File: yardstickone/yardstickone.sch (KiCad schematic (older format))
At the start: 68 parts, among them J1 USB-DEVICE, P1 CONN_02X07, P2 SMA-EDGE, P3 RESET_N, P4 DD, P5 DC, P6 3V3, P7 GND, T1 BALUN, U1 CC1111, U2 AP7313, U3 DMC2400, U4 RX_AMP, U5 SKY13385, U6 SKY13385, U7 TX_AMP, U8 DMC2400, X1 CRYSTAL

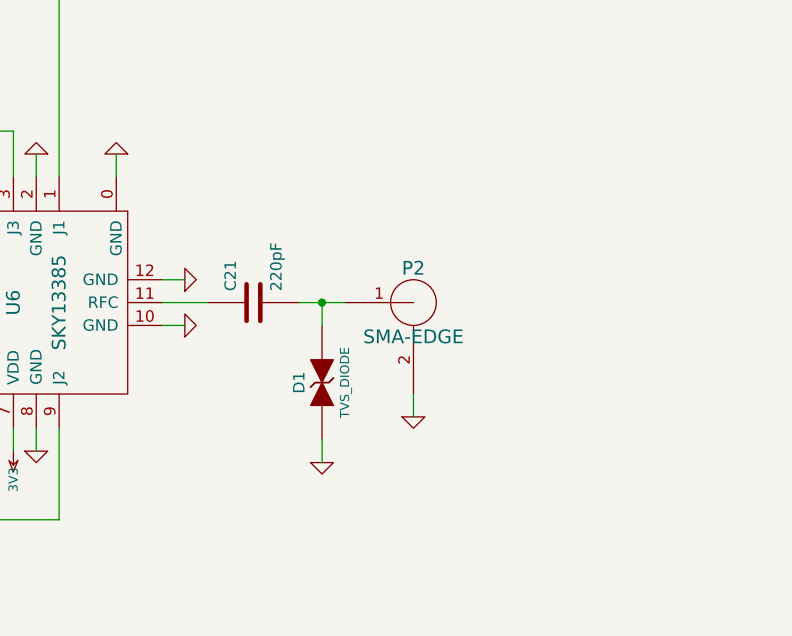
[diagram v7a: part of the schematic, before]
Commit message: added 900 MHz low pass filter
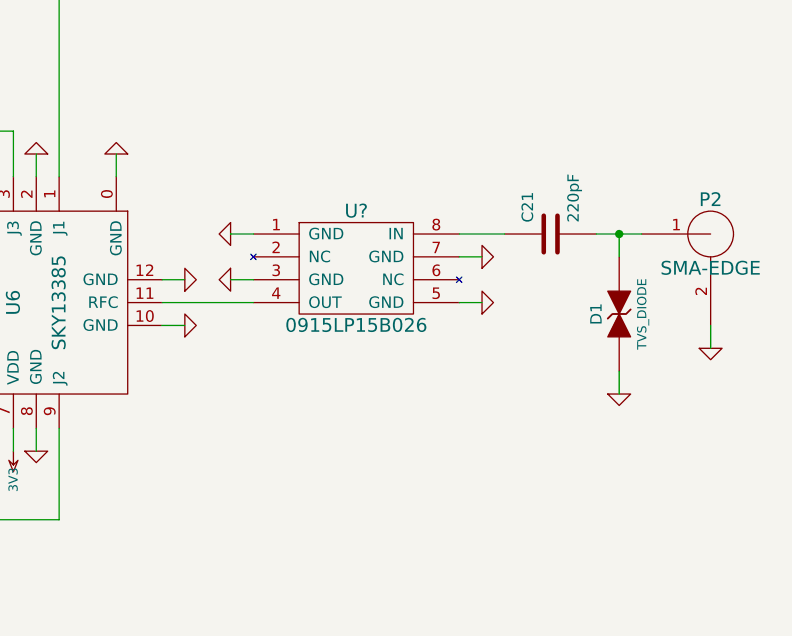
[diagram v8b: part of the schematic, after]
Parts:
- added U?: 0915LP15B026, symbol 0915LP15B026
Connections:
- net GND: now also U?.1 (GND), U?.3 (GND), U?.5 (GND), U?.7 (GND)
- net at U6.11 (RFC): now also U?.4 (OUT); no longer C21.1
- new net: C21.1, U?.8 (IN)
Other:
- moved on the sheet: C21, D1, P2
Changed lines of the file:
@@
 	11750 7800 11750 8000
 Wire Wire Line
-	13400 5450 13600 5450
-Wire Wire Line
 	9650 4500 9650 6300
 Wire Wire Line
@@
 Wire Wire Line
 	1700 3700 1700 3600
-Connection ~ 14100 5450
-Wire Wire Line
-	14000 5450 14200 5450
-Wire Wire Line
-	14100 6150 14100 6050
+Connection ~ 15400 5150
+Wire Wire Line
+	15300 5150 15500 5150
+Wire Wire Line
+	15400 5850 15400 5750
 Wire Wire Line
 	4650 3050 4650 2850
@@
 	5450 5550 5450 5050
 Wire Wire Line
-	14100 5550 14100 5450
+	15400 5250 15400 5150
 Wire Wire Line
 	5350 5550 5350 5050
@@
 L C C21
 U 1 1 50A179AF
-P 13800 5450
-F 0 "C21" H 13850 5550 50  0000 L CNN
-F 1 "220pF" H 13850 5350 50  0000 L CNN
-F 2 "cc1111-legacy:GSG-0402" H 13800 5450 60  0001 C CNN
-F 3 "" H 13800 5450 60  0001 C CNN
-F 4 "Murata" H 13800 5450 60  0001 C CNN "Manufacturer"
-F 5 "GRM155R71H221KA01D" H 13800 5450 60  0001 C CNN "Part Number"
-F 6 "CAP CER 220PF 50V 10% X7R 0402" H 13800 5450 60  0001 C CNN "Description"
-	1    13800 5450
+P 15100 5150
+F 0 "C21" H 15150 5250 50  0000 L CNN
+F 1 "220pF" H 15150 5050 50  0000 L CNN
+F 2 "cc1111-legacy:GSG-0402" H 15100 5150 60  0001 C CNN
+F 3 "" H 15100 5150 60  0001 C CNN
+F 4 "Murata" H 15100 5150 60  0001 C CNN "Manufacturer"
+F 5 "GRM155R71H221KA01D" H 15100 5150 60  0001 C CNN "Part Number"
+F 6 "CAP CER 220PF 50V 10% X7R 0402" H 15100 5150 60  0001 C CNN "Description"
+	1    15100 5150
 	0    -1   -1   0
 $EndComp
@@
 L GND #PWR02
 U 1 1 50A0885D
-P 14500 5950
-F 0 "#PWR02" H 14500 5950 30  0001 C CNN
-F 1 "GND" H 14500 5880 30  0001 C CNN
-F 2 "" H 14500 5950 60  0001 C CNN
-F 3 "" H 14500 5950 60  0001 C CNN
-	1    14500 5950
+P 15800 5650
+F 0 "#PWR02" H 15800 5650 30  0001 C CNN
+F 1 "GND" H 15800 5580 30  0001 C CNN
+F 2 "" H 15800 5650 60  0001 C CNN
+F 3 "" H 15800 5650 60  0001 C CNN
+	1    15800 5650
 	1    0    0    -1
 $EndComp
@@
 L RF-CONN P2
 U 1 1 50A0883B
-P 14500 5450
-F 0 "P2" H 14500 5600 60  0000 C CNN
-F 1 "SMA-EDGE" H 14500 5300 60  0000 C CNN
-F 2 "cc1111-legacy:GSG-SMA-EDGE" H 14500 5450 60  0001 C CNN
-F 3 "" H 14500 5450 60  0001 C CNN
-F 4 "Linx Technologies" H 14500 5450 60  0001 C CNN "Manufacturer"
-F 5 "CONSMA003.062" H 14500 5450 60  0001 C CNN "Part Number"
-F 6 "CONN SMA JACK 50 OHM EDGE MNT" H 14500 5450 60  0001 C CNN "Description"
-	1    14500 5450
+P 15800 5150
+F 0 "P2" H 15800 5300 60  0000 C CNN
+F 1 "SMA-EDGE" H 15800 5000 60  0000 C CNN
+F 2 "cc1111-legacy:GSG-SMA-EDGE" H 15800 5150 60  0001 C CNN
+F 3 "" H 15800 5150 60  0001 C CNN
+F 4 "Linx Technologies" H 15800 5150 60  0001 C CNN "Manufacturer"
+F 5 "CONSMA003.062" H 15800 5150 60  0001 C CNN "Part Number"
+F 6 "CONN SMA JACK 50 OHM EDGE MNT" H 15800 5150 60  0001 C CNN "Description"
+	1    15800 5150
 	-1   0    0    -1
 $EndComp
@@
 L GND #PWR043
 U 1 1 504CFCE4
-P 14100 6150
-F 0 "#PWR043" H 14100 6150 30  0001 C CNN
-F 1 "GND" H 14100 6080 30  0001 C CNN
-F 2 "" H 14100 6150 60  0001 C CNN
-F 3 "" H 14100 6150 60  0001 C CNN
-	1    14100 6150
+P 15400 5850
+F 0 "#PWR043" H 15400 5850 30  0001 C CNN
+F 1 "GND" H 15400 5780 30  0001 C CNN
+F 2 "" H 15400 5850 60  0001 C CNN
+F 3 "" H 15400 5850 60  0001 C CNN
+	1    15400 5850
 	1    0    0    -1
 $EndComp
@@
 L GSG-DIODE-TVS-BI D1
 U 1 1 504CFCBE
-P 14100 5800
-F 0 "D1" H 14100 5900 50  0000 C CNN
-F 1 "TVS_DIODE" H 14100 5700 40  0000 C CNN
-F 2 "cc1111-legacy:GSG-0402" H 14100 5800 60  0001 C CNN
-F 3 "" H 14100 5800 60  0001 C CNN
-F 4 "Murata" H 14100 5800 60  0001 C CNN "Manufacturer"
-F 5 "LXES15AAA1-100" H 14100 5800 60  0001 C CNN "Part Number"
-F 6 "TVS DIODE ESD .05PF 15KV 0402" H 14100 5800 60  0001 C CNN "Description"
-	1    14100 5800
+P 15400 5500
+F 0 "D1" H 15400 5600 50  0000 C CNN
+F 1 "TVS_DIODE" H 15400 5400 40  0000 C CNN
+F 2 "cc1111-legacy:GSG-0402" H 15400 5500 60  0001 C CNN
+F 3 "" H 15400 5500 60  0001 C CNN
+F 4 "Murata" H 15400 5500 60  0001 C CNN "Manufacturer"
+F 5 "LXES15AAA1-100" H 15400 5500 60  0001 C CNN "Part Number"
+F 6 "TVS DIODE ESD .05PF 15KV 0402" H 15400 5500 60  0001 C CNN "Description"
+	1    15400 5500
 	0    -1   -1   0
 $EndComp
@@
 	14200 3450 14200 3550
 Wire Wire Line
-	14500 5850 14500 5950
+	15800 5550 15800 5650
 $Comp
 L CONN_02X07 P1
@@
 Wire Wire Line
 	10500 2450 10500 2550
+$Comp
+L 0915LP15B026 U?
+U 1 1 54E3F891
+P 14250 5300
+F 0 "U?" H 14250 5550 60  0000 C CNN
+F 1 "0915LP15B026" H 14250 5050 60  0000 C CNN
+F 2 "" H 14250 5300 60  0000 C CNN
+F 3 "" H 14250 5300 60  0000 C CNN
+	1    14250 5300
+	1    0    0    -1
+$EndComp
+$Comp
+L GND #PWR?
+U 1 1 54E40330
+P 13700 5350
+F 0 "#PWR?" H 13700 5350 30  0001 C CNN
+F 1 "GND" H 13700 5280 30  0001 C CNN
+F 2 "" H 13700 5350 60  0000 C CNN
+F 3 "" H 13700 5350 60  0000 C CNN
+	1    13700 5350
+	0    1    1    0
+$EndComp
+$Comp
+L GND #PWR?
+U 1 1 54E405AF
+P 13700 5150
+F 0 "#PWR?" H 13700 5150 30  0001 C CNN
+F 1 "GND" H 13700 5080 30  0001 C CNN
+F 2 "" H 13700 5150 60  0000 C CNN
+F 3 "" H 13700 5150 60  0000 C CNN
+	1    13700 5150
+	0    1    1    0
+$EndComp
+$Comp
+L GND #PWR?
+U 1 1 54E405FF
+P 14800 5450
+F 0 "#PWR?" H 14800 5450 30  0001 C CNN
+F 1 "GND" H 14800 5380 30  0001 C CNN
+F 2 "" H 14800 5450 60  0000 C CNN
+F 3 "" H 14800 5450 60  0000 C CNN
+	1    14800 5450
+	0    -1   -1   0
+$EndComp
+$Comp
+L GND #PWR?
+U 1 1 54E4064F
+P 14800 5250
+F 0 "#PWR?" H 14800 5250 30  0001 C CNN
+F 1 "GND" H 14800 5180 30  0001 C CNN
+F 2 "" H 14800 5250 60  0000 C CNN
+F 3 "" H 14800 5250 60  0000 C CNN
+	1    14800 5250
+	0    -1   -1   0
+$EndComp
+Wire Wire Line
+	14800 5250 14700 5250
+Wire Wire Line
+	14700 5450 14800 5450
+Wire Wire Line
+	13800 5150 13700 5150
+Wire Wire Line
+	13700 5350 13800 5350
+Wire Wire Line
+	13800 5450 13400 5450
+Wire Wire Line
+	14700 5150 14900 5150
 $EndSCHEMATC
